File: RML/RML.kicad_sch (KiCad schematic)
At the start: 29 parts, among them Q101 Q_NMOS_GDS, Q102 Q_NMOS_GDS, U101 641964-1, U102 LM555xM, U103 SFH617A-1, U104 74AHC1G02, U105 641964-1, U106 641964-1, U107 LM7805_TO220

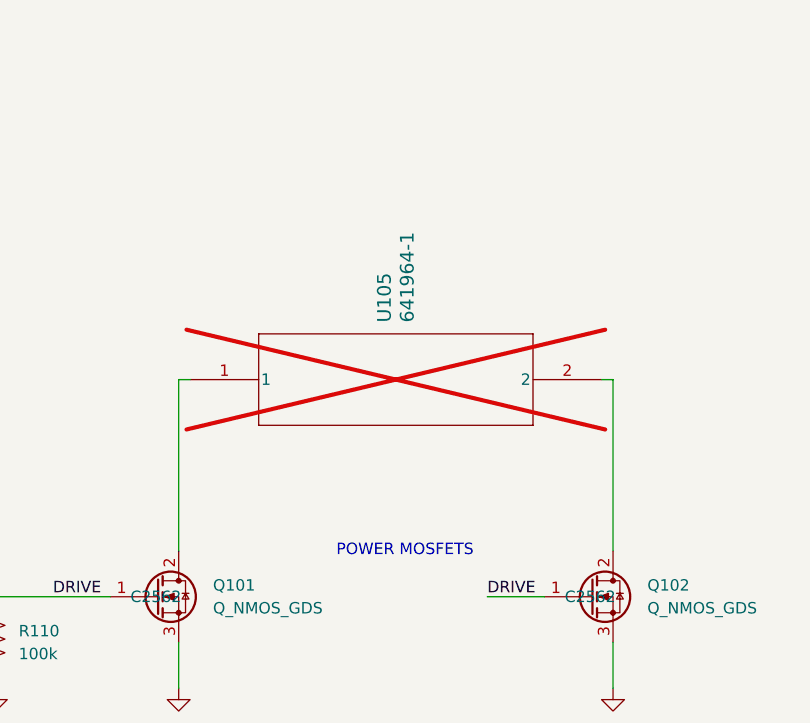
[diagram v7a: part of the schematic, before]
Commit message: Fixed RML footprint issues
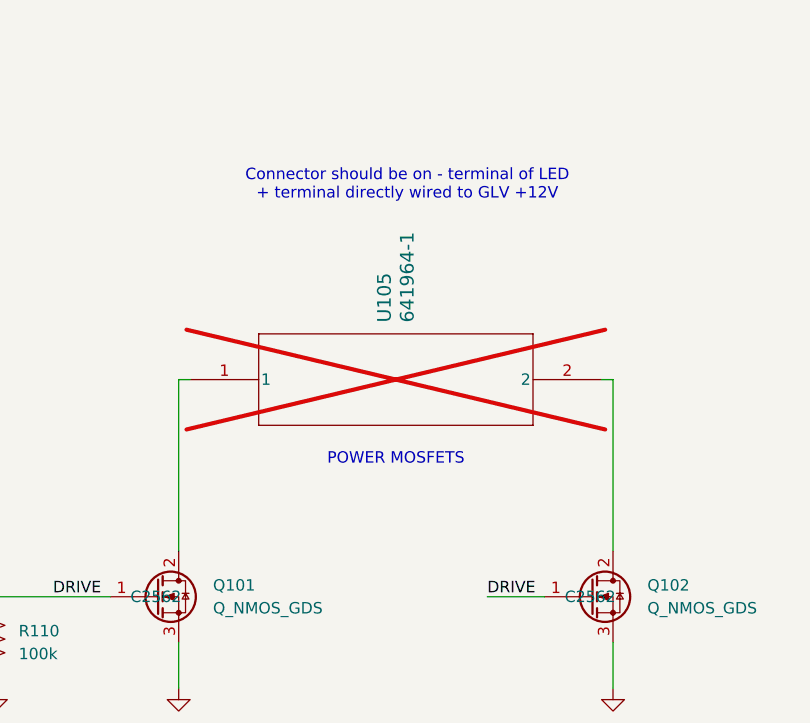
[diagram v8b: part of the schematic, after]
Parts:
- C101: footprint Capacitor_SMD:C_0201_0603Metric -> Capacitor_SMD:C_0603_1608Metric
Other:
- note added: "Connector should be on - terminal of LED + terminal directly wired to GLV +12V"
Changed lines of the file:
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@@
 	(text "POWER MOSFETS"
 		(exclude_from_sim no)
-		(at 266.446 81.28 0)
+		(at 265.43 71.12 0)
+		(effects
+			(font
+				(size 1.27 1.27)
+			)
+		)
+	)
+	(text "Connector should be on - terminal of LED\n+ terminal directly wired to GLV +12V"
+		(exclude_from_sim no)
+		(at 266.7 40.64 0)
 		(effects
 			(font
@@
 	(wire
 		(pts
+			(xy 241.3 62.23) (xy 242.57 62.23)
+		)
+		(stroke
+			(width 0)
+			(type default)
+		)
+	)
+	(wire
+		(pts
 			(xy 220.98 87.63) (xy 220.98 86.36)
 		)
@@
 	(wire
 		(pts
-			(xy 242.57 62.23) (xy 241.3 62.23)
-		)
-		(stroke
-			(width 0)
-			(type default)
-		)
-	)
-	(wire
-		(pts
 			(xy 189.23 97.79) (xy 189.23 96.52)
 		)
@@
 			"dABzAD4ADQANAAoAPAAvAGQAdQBpAHgAbQBsAD4ADQANAAoAAAD/////////////////////////"
 			"/////////////////1oBAFs0ZQ8AgK7RPhACAABwfGY5EAIAAP//////////////////////////"
-			"/////////////////////w=="
+			"/////////////////////wAAAAAAAAAAAAAAAAAAAAAAAAAAAAAAAAAAAAAAAAAAAAAAAAAAAAAA"
+			"AAAAAAAAAAAAAAAAAAAAAAAAAAAAAAAAAAAAAAAAAAAAAAAAAAAAAAAAAAAAAAAAAAAAAAAAAAAA"
+			"AAAAAAAAAAAAAAAAAAAAAAAAAAAAAAAAAAAAAAAAAAAAAAAAAAAAAAAAAAAAAAAAAAAAAAAAAAAA"
+			"AAAAAAAAAAAAAAAAAAAAAAAAAAAAAAAAAAAAAAAAAAAAAAAAAAAAAAAAAAAAAAAAAAAAAAAAAAAA"
+			"AAAAAAAAAAAAAAAAAAAAAAAAAAAAAAAAAAAAAAAAAAAAAAAAAAAAAAAAAAAAAAAAAAAAAAAAAAAA"
+			"AAAAAAAAAAAAAAAAAAAAAAAAAAAAAAAAAAAAAAAAAAAAAAAAAAAAAAAAAAAAAAAAAAAAAAAAAAAA"
+			"AAAAAAAAAAAAAAAAAAAAAAAAAAAAAAAAAAAAAAAAAAAAAAAAAAAAAAAAAAAAAAAAAAAAAAAAAAAA"
+			"AAAAAAAAAAAAAAAAAAAAAAAAAAAAAAAAAAAAAAAAAAAAAAAAAAAAAAAAAAAAAAAAAAAAAAAAAAAA"
+			"AAAAAAAAAAAAAAAAAAAAAAAAAAAAAAAAAAAAAAAAAAAAAAAAAAAAAAAAAAAAAAAAAAAAAAAAAAAA"
+			"AAAAAAAAAAAAAAAAAAAAAAAAAAAAAAAAAAAAAAAAAAAAAAAAAAAAAAAAAAAAAAAAAAAAAAAAAAAA"
+			"AAAAAAAAAAAAAAAAAAAAAAAAAAAAAAAAAAAAAAAAAAAAAAAAAAAAAAAAAAAAAAAAAAAAAAAAAAAA"
+			"AAAAAAAAAAAAAAAAAAAAAAAAAAAAAAAAAAAAAAAAAAAAAAAAAAAAAAAAAAAAAAAAAAAAAAAAAAAA"
+			"AAAAAAAAAAAAAAAAAAAAAAAAAAAAAAAAAAAAAAAAAAAAAAAAAAAAAAAAAAAAAAAAAAAAAAAAAAAA"
+			"AAAAAAAAAAAAAAAAAAAAAAAAAAAAAAAAAAAAAAAAAAAAAAAAAAAAAAAAAAAAAAAAAAAAAAAAAAAA"
+			"AAAAAAAAAAAAAAAAAAAAAAAAAAAAAAAAAAAAAAAAAAAAAAAAAAAAAAAAAAAAAAAAAAAAAAAAAAAA"
+			"AAAAAAAAAAAAAAAAAAAAAAAAAAAAAAAAAAAAAAAAAAAAAAAAAAAAAAAAAAAAAAAAAAAAAAAAAAAA"
+			"AAAAAAAAAAAAAAAAAAAAAAAAAAAAAAAAAAAAAAAAAAAAAAAAAAAAAAAAAAAAAAAAAAAAAAAAAAAA"
+			"AAAAAAAAAAAAAAAAAAAAAAAAAAAAAAAAAAAAAAAAAAAAAAAAAAAAAAAAAAAAAAAAAAAAAAAAAAAA"
+			"AAAAAAAAAAAAAAAAAAAAAA=="
 		)
 	)
@@
 			)
 		)
-		(property "Footprint" "Capacitor_SMD:C_0201_0603Metric"
+		(property "Footprint" "Capacitor_SMD:C_0603_1608Metric"
 			(at 46.99 153.67 0)
 			(effects
